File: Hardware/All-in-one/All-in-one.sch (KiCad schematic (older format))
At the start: 14 parts, among them J1 Conn_01x04_Male, J2 Barrel_Jack, J3 Conn_01x03, J4 Conn_01x02_Male, J5 Conn_01x02_Male, J7 Conn_01x02_Male, J8 Conn_01x02_Male, U2 BMP280_flipped, U3 YAAJ_BluePill_Part_Like, U4 microSD_flipped

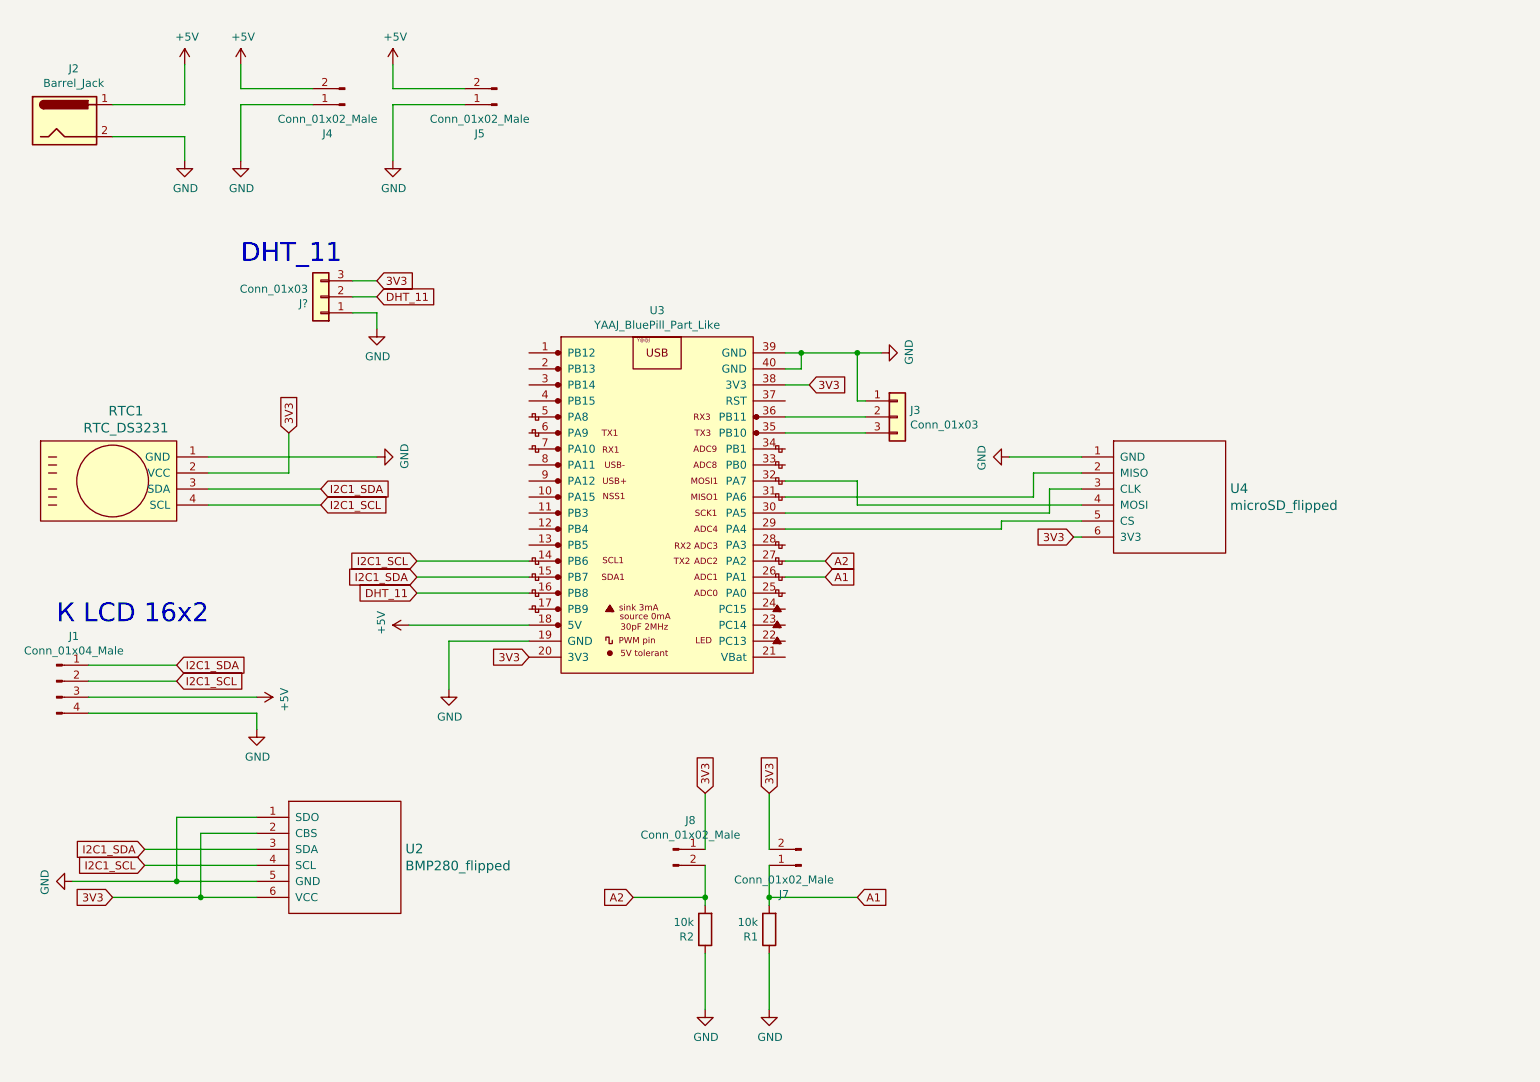
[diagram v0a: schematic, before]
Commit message: Добавлена четвёртая кнопка "X10" на вывод PA15
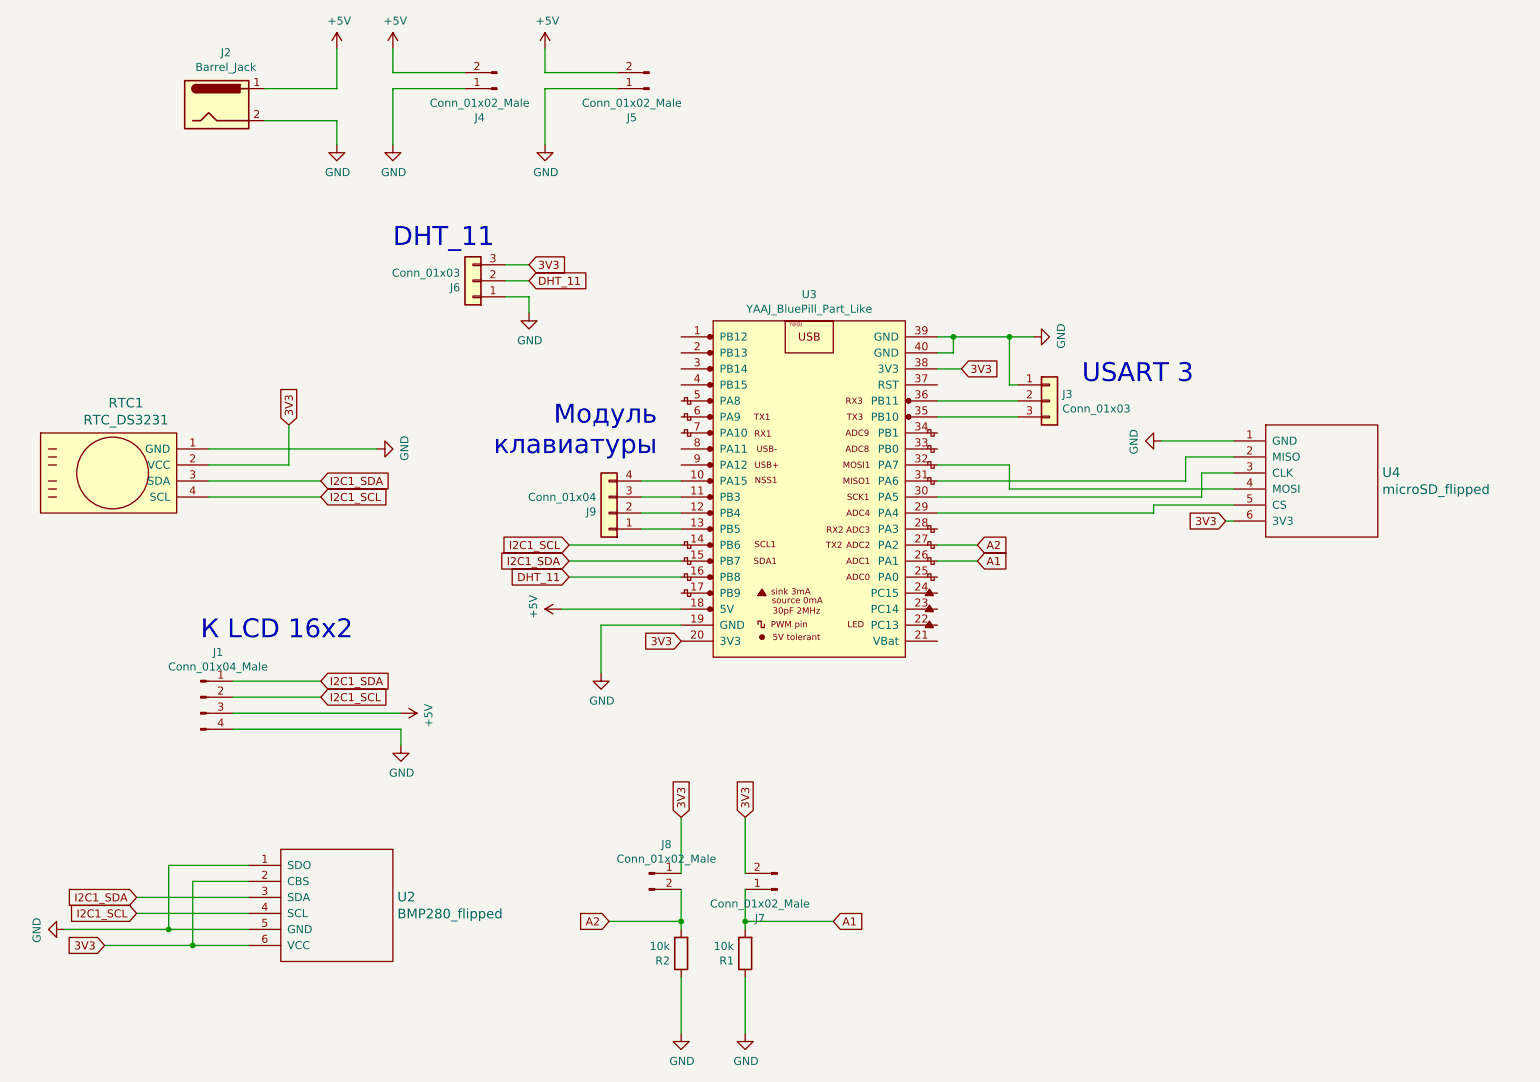
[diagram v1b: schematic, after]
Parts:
- added J9: Conn_01x04, Connector_PinHeader_2.54mm:PinHeader_1x04_P2.54mm_Vertical, symbol Connector_Generic:Conn_01x04
- gave numbers to parts that had none: 1
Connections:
- net at U3.10 (PA15): now also J9.4 (Pin_4)
- net at U3.11 (PB3): now also J9.3 (Pin_3)
- net at U3.12 (PB4): now also J9.2 (Pin_2)
- net at U3.13 (PB5): now also J9.1 (Pin_1)
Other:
- note added: "USART 3"
- note added: "Модуль\nклавиатуры"
- moved on the sheet: J1, J2, J3, J4, J5, J6, J7, J8, R1, R2, RTC1, U2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
